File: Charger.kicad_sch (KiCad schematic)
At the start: 75 parts, among them J2 Conn_02x04_Odd_Even, J4 Conn_02x05_Odd_Even, Q6 BSC0702LS, Q7 BSC0702LS, Q8 BSC0702LS, Q9 BSC0702LS, U27 BQ25756RRVR

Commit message: Add FT rotations and kibot filter and set fuses DNP
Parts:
- J2, J4: FT Rotation Offset (none) -> 90
- U27: FT Rotation Offset (none) -> -90
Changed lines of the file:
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@@
 			)
 		)
-		(property "APPLICATION" ""
+		(property "FT Rotation Offset" "-90"
 			(at 165.1 143.51 0)
 			(effects
@@
 			)
 		)
-		(property "Field4" ""
+		(property "FT Rotation Offset" "90"
 			(at 105.41 208.28 0)
 			(effects
@@
 			)
 		)
-		(property "Field4" ""
+		(property "FT Rotation Offset" "90"
 			(at 299.72 182.88 0)
 			(effects

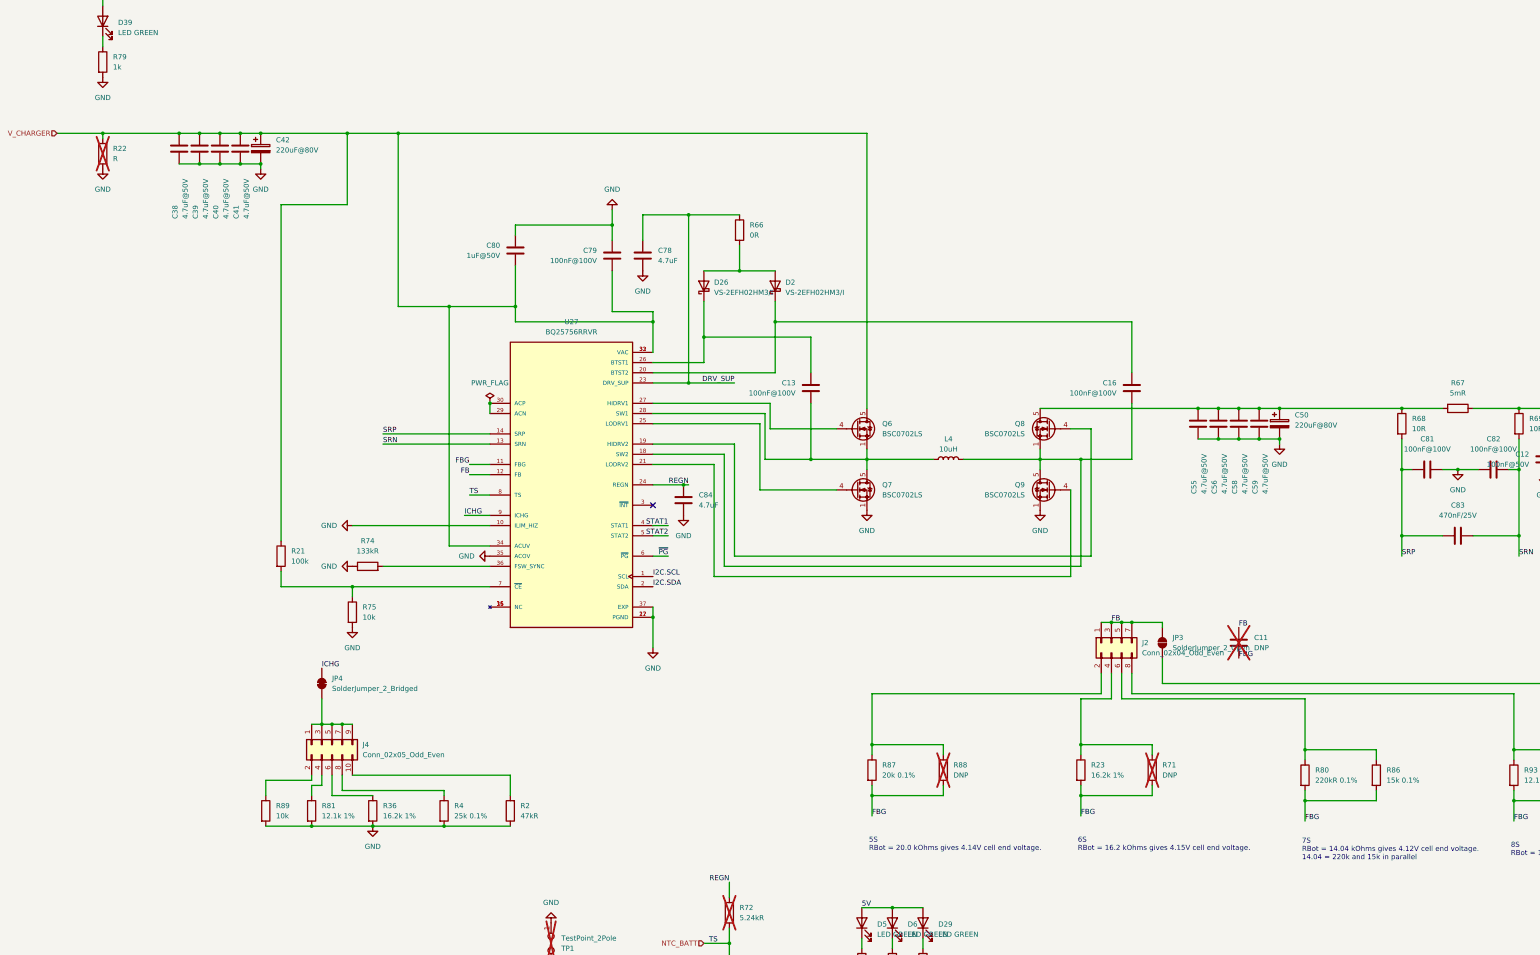
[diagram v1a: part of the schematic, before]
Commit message: Add AC-Sense
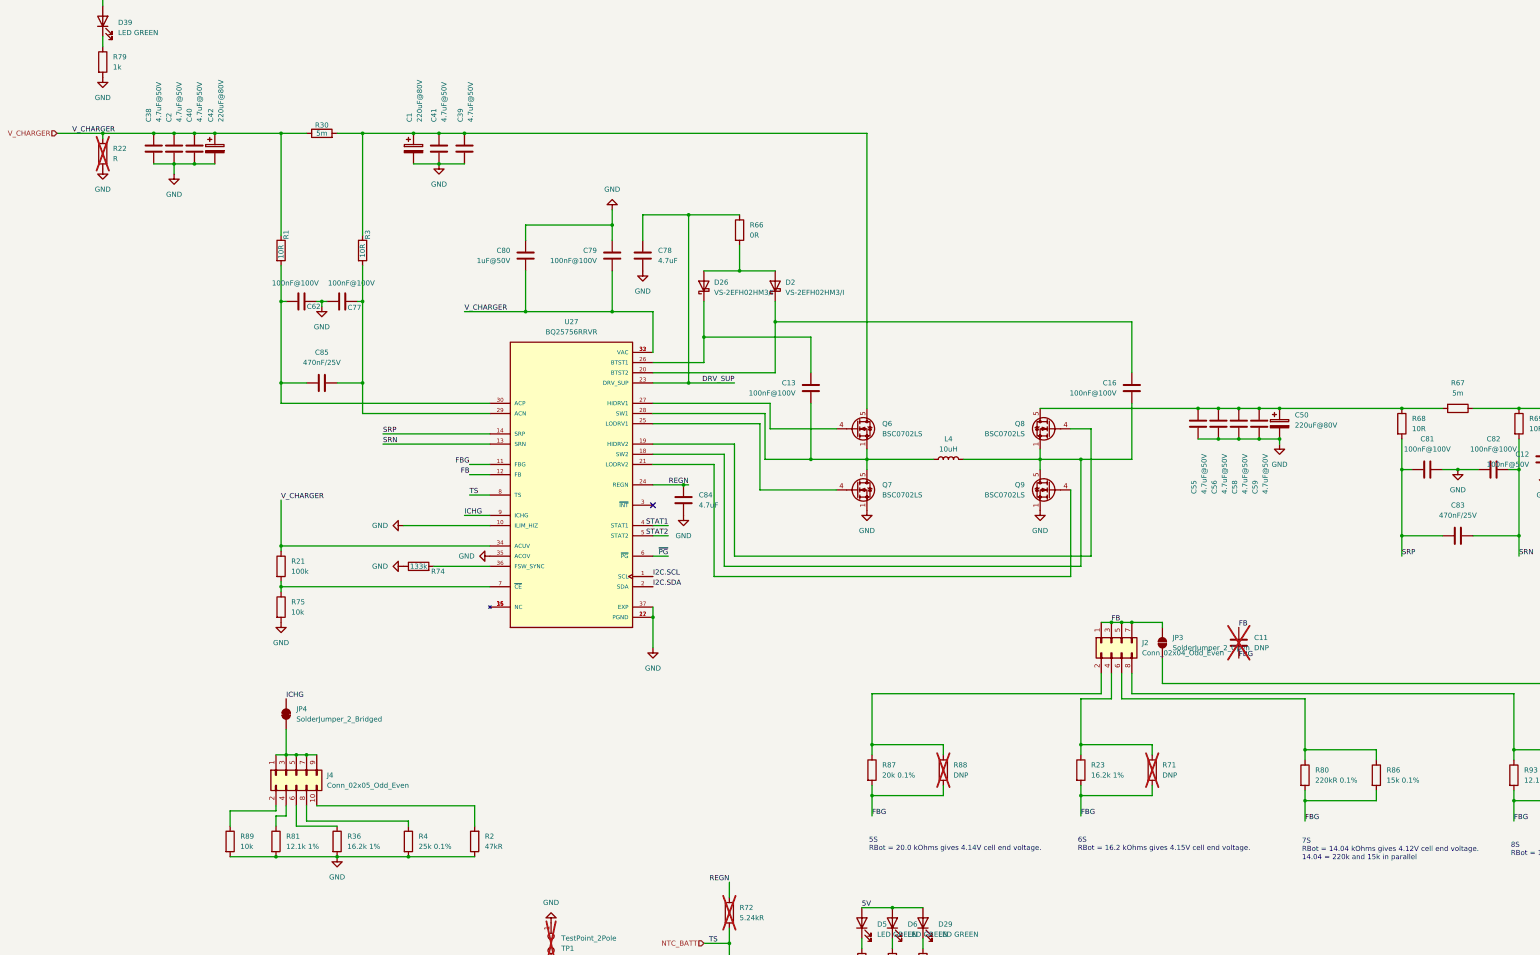
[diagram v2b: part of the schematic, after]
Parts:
- added C1: 220uF@80V, Capacitor_THT:CP_Radial_D10.0mm_P5.00mm, symbol Device:C_Polarized
- added C2: 4.7uF@50V, Capacitor_SMD:C_1206_3216Metric, symbol Device:C
- added C62, C77: 100nF@100V, Capacitor_SMD:C_0805_2012Metric, symbol Device:C
- added C85: 470nF/25V, Capacitor_SMD:C_0603_1608Metric, symbol Device:C
- added R1, R3: 10R, Resistor_SMD:R_0603_1608Metric, symbol Device:R
- added R30: 5m, Resistor_SMD:R_2512_6332Metric, symbol Device:R
- R67: value 5mR -> 5m; JLC C309526 -> C185817
- R74: value 133kR -> 133k
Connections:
- net GND: now also C1.2, C2.2, C62.2, C77.1
- net V_CHARGER: now also C2.1, R1.1, R30.1; no longer C39.1, C41.1, Q6.5 (D)
- net at U27.29 (ACN): now also C77.2, C85.1, R3.2; no longer U27.30 (ACP)
- new net: C62.1, C85.2, R1.2, U27.30 (ACP)
- new net: C1.1, C39.1, C41.1, Q6.5 (D), R3.1, R30.2
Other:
- moved on the sheet: C38, C39, C40, C41, C42, C80, J4, JP4, R2, R21, R36, R4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

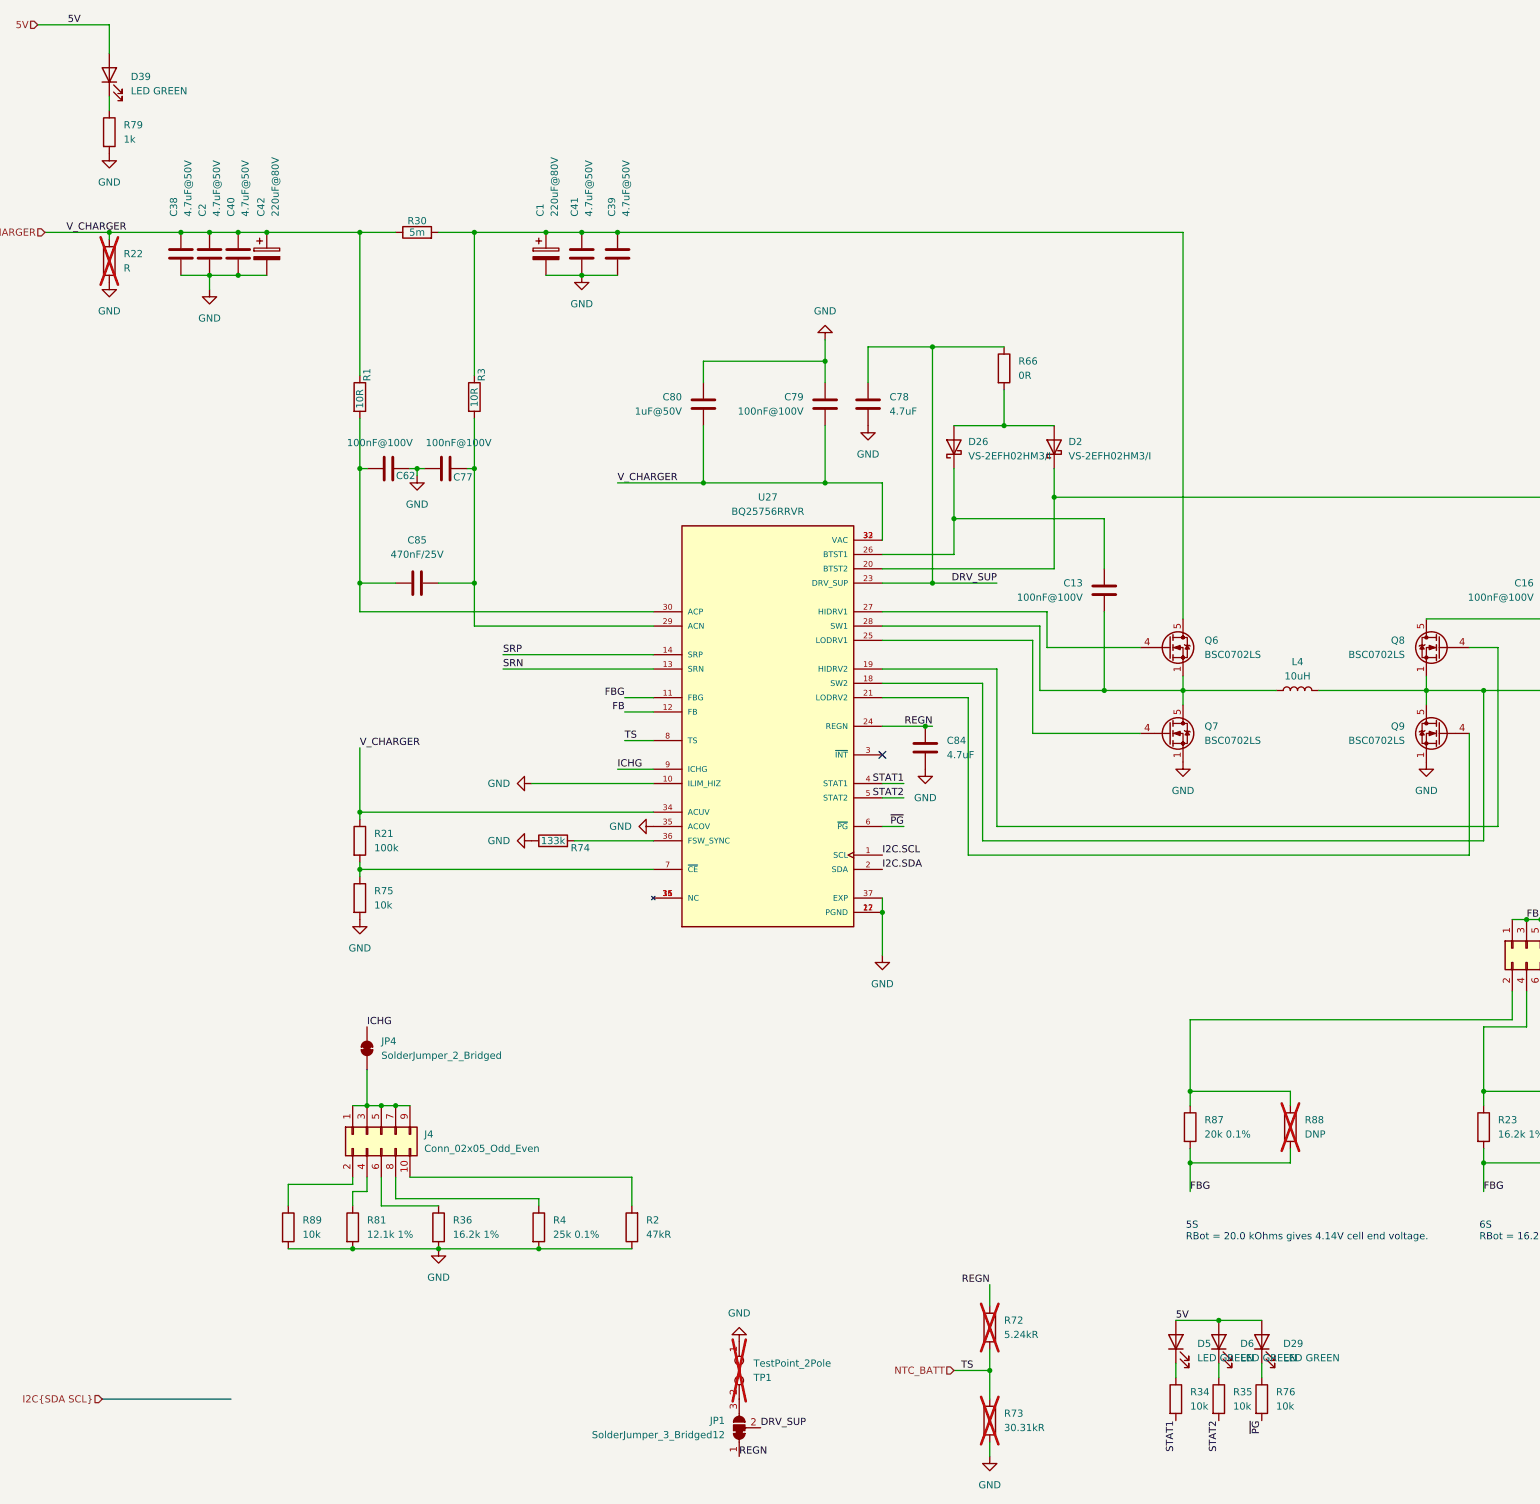
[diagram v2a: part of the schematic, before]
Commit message: Add /CE, NTC Selector, 5V LDO. Fix copper traces, vias in pads and this and that
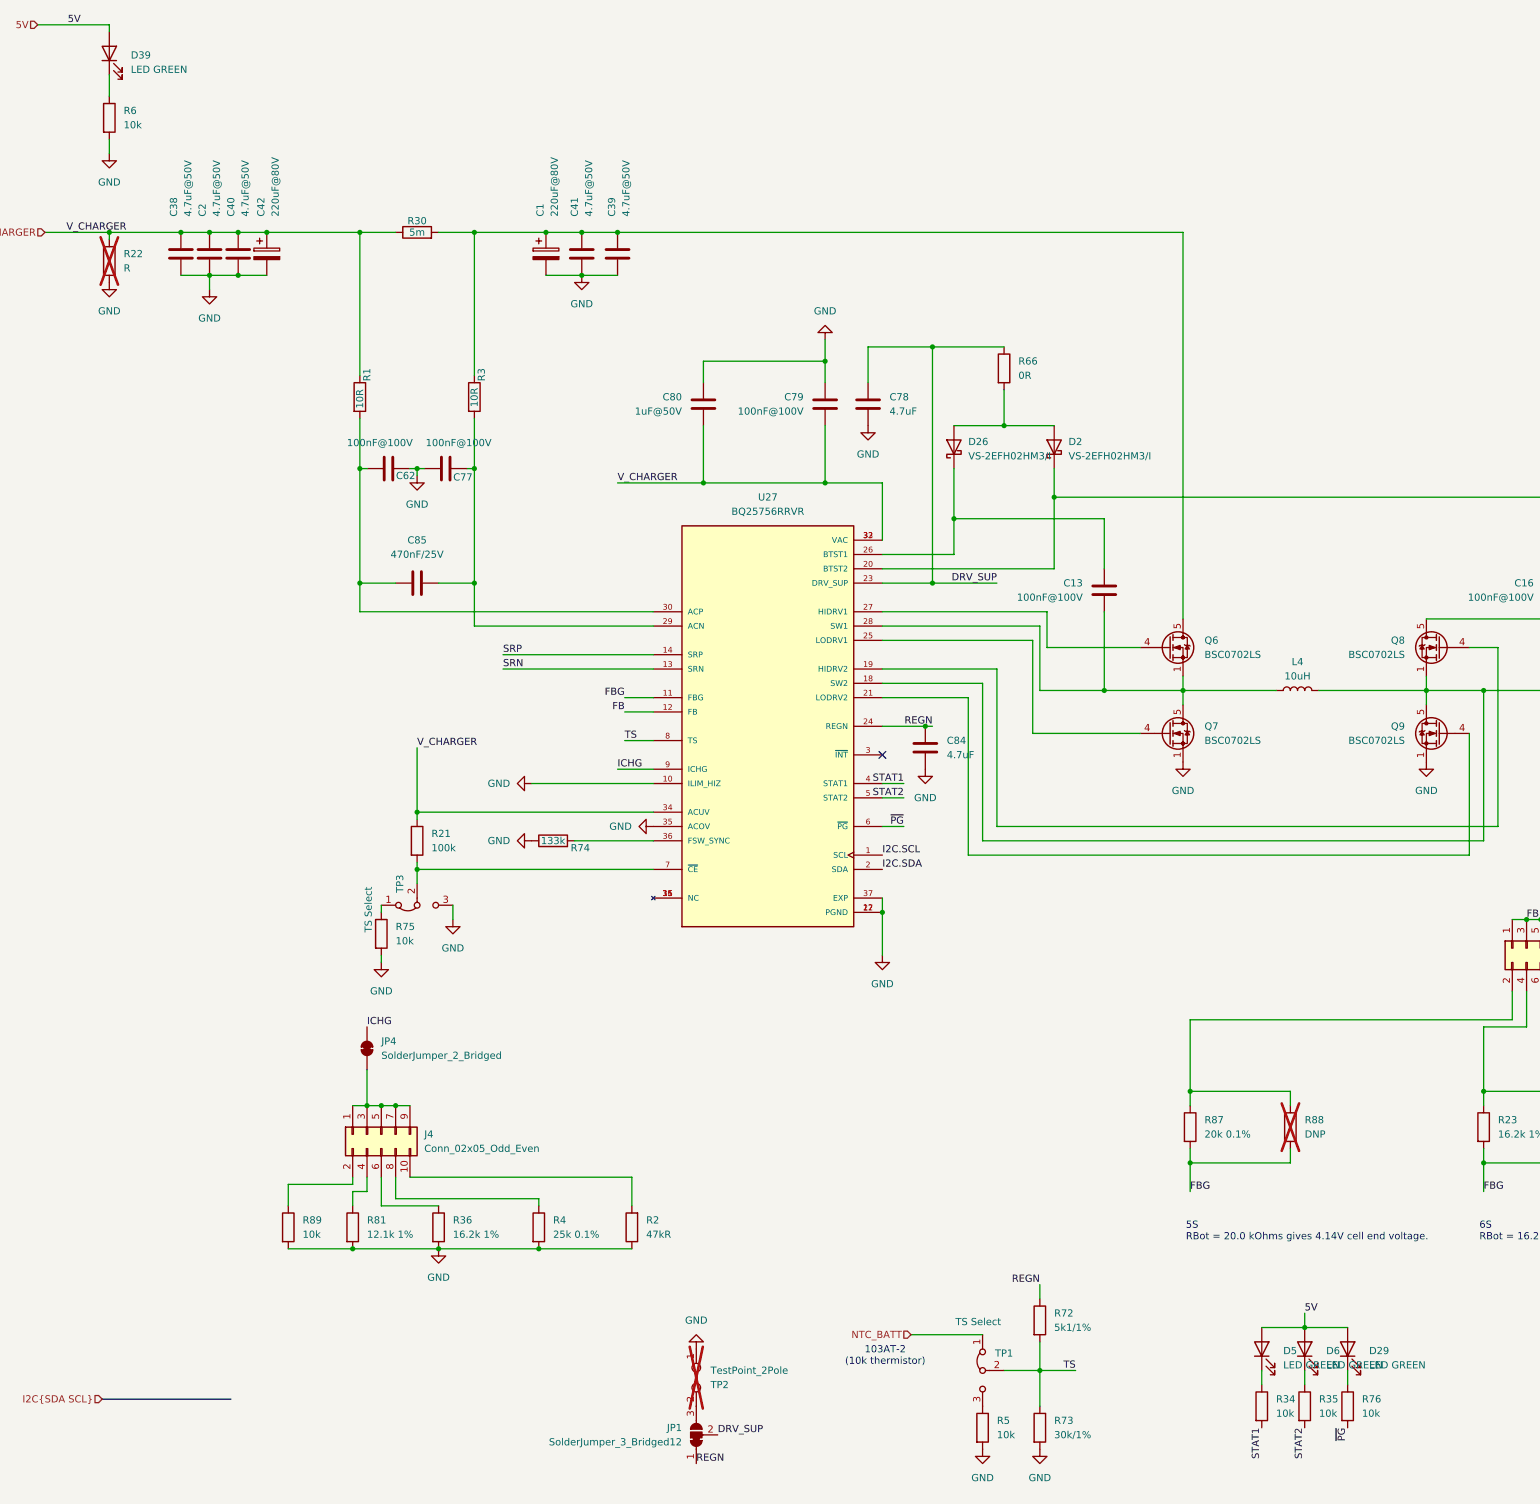
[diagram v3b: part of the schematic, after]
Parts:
- removed R79: 1k, Resistor_SMD:R_0805_2012Metric, symbol Device:R
- added R5, R6: 10k, Resistor_SMD:R_0402_1005Metric, symbol Device:R
- added TP2: TestPoint_2Pole, Connector_PinHeader_2.54mm:PinHeader_1x02_P2.54mm_Vertical, symbol Connector:TestPoint_2Pole
- added TP3: TS Select, Connector_PinHeader_2.54mm:PinHeader_1x03_P2.54mm_Vertical, symbol Jumper:Jumper_3_Bridged12
- R72: value 5.24kR -> 5k1/1%; JLC (none) -> C23186; now fitted
- R73: value 30.31kR -> 30k/1%; JLC (none) -> C22984; now fitted
- TP1: value TestPoint_2Pole -> TS Select; footprint Connector_PinHeader_2.54mm:PinHeader_1x02_P2.54mm_Vertical -> Connector_PinHeader_2.54mm:PinHeader_1x03_P2.54mm_Vertical; symbol Connector:TestPoint_2Pole -> Jumper:Jumper_3_Bridged12; JLC (none) -> C49257; now fitted
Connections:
- net GND: now also R5.2, R6.2, TP2.1, TP3.3 (B); no longer TP1.1
- net NTC_BATT: now also TP1.1 (A); no longer R72.2, R73.1, U27.8 (TS)
- net at R21.2, U27.7 (~{CE}): now also TP3.2 (C); no longer R75.1
- net at D39.1 (K): now also R6.1
- net at JP1.3 (B): now also TP2.2; no longer TP1.2
- new net: R75.1, TP3.1 (A)
- new net: R5.1, TP1.3 (B)
- new net TS: R72.2, R73.1, TP1.2 (C), U27.8 (TS)
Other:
- note added: "103AT-2 (10k thermistor)"
- title: OpenMower Charger -> Charger
- moved on the sheet: D29, D39, D5, D6, JP1, R21, R34, R35, R75, R76

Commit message: Fixed CE pin connection; Use git version as variable
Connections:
- net at R21.2, TP3.2 (C), U27.7 (~{CE}): now also R75.1
- net at TP3.1 (A): no longer R75.1
- no-connect marks 1 -> 2
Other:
- moved on the sheet: R75
